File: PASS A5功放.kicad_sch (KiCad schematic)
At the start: 43 parts, among them IC1 OPA1611AIDR, IC2 LM317AEMPX_NOPB, IC3 LM337IMP_NOPB, U1 UPC1237HA, U2 SFH6206-2T

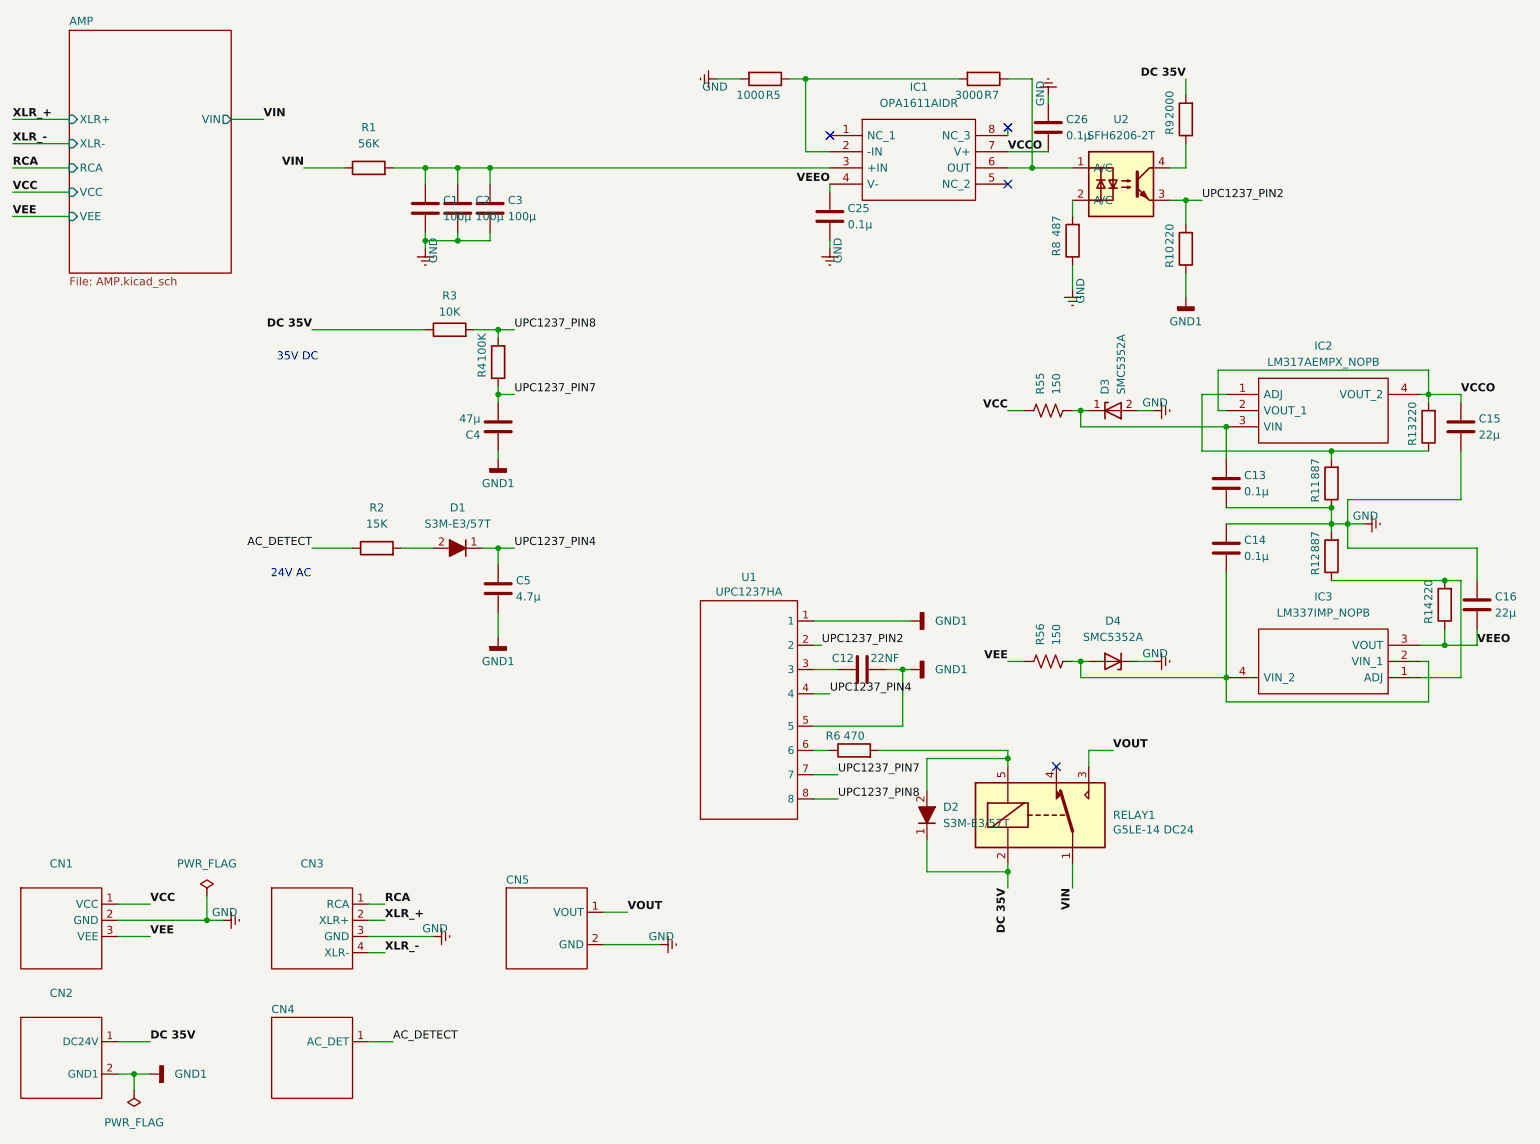
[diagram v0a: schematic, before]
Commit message: using SMD power resistor
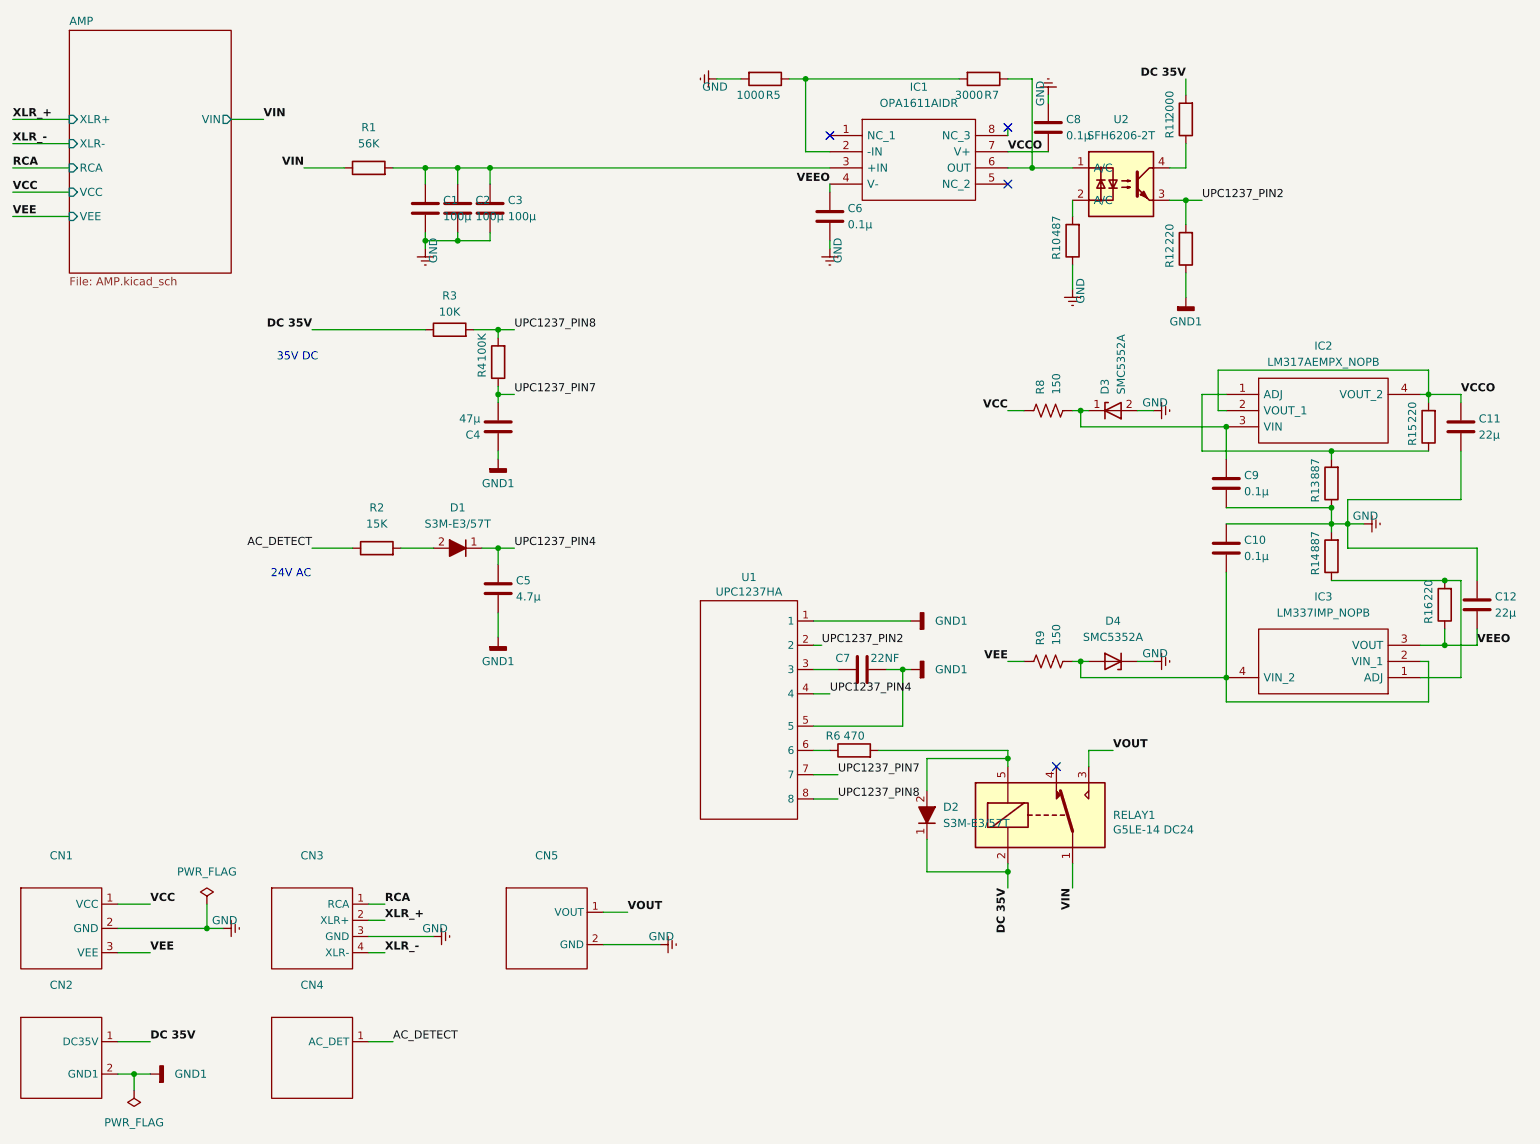
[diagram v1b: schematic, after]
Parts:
- removed CN1, CN3: ~, connectors:4线焊盘, symbol CN:CN-VIN
- removed CN2: ~, connectors:2线焊盘, symbol CN:2线焊盘
- removed CN4, CN5: ~, connectors:2线焊盘, symbol CN:CN-OUT
- added CN1: ~, connectors:3线焊盘, symbol cus_connector:3线焊盘
- added CN2, CN5: ~, connectors:2线焊盘, symbol cus_connector:2线焊盘
- added CN3: ~, connectors:4线焊盘, symbol cus_connector:4线焊盘
- added CN4: ~, connectors:1线焊盘, symbol cus_connector:1线焊盘
- R8: renamed from R55; footprint cus_resistor:RSF5SSJT-73-150R_Vertical -> cus_resistor:SMW 5W 150R J
- R9: renamed from R56; footprint cus_resistor:RSF5SSJT-73-150R_Vertical -> cus_resistor:SMW 5W 150R J
- renumbered C14 to C10, C15 to C11, C16 to C12, C25 to C6, C12 to C7, C26 to C8, C13 to C9, R8 to R10, R9 to R11, R10 to R12, R11 to R13, R12 to R14, R13 to R15, R14 to R16
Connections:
- net AC_DETECT: now also CN4.1 (AC_DET)
- net DC 35V: now also CN2.1 (DC35V)
- net GND: now also CN1.2 (GND), CN3.3 (GND), CN5.2 (GND)
- net GND1: now also CN2.2 (GND1)
- net RCA: now also CN3.1 (RCA)
- net VCC: now also CN1.1 (VCC)
- net VEE: now also CN1.3 (VEE)
- net VOUT: now also CN5.1 (VOUT)
- net XLR_+: now also CN3.2 (XLR+)
- net XLR_-: now also CN3.4 (XLR-)
